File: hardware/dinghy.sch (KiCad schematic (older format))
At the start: 56 parts, among them J10 Header 1, J11 Header 2, J2 Fan 1, J3 Fan2, J4 Motor, J5 Endtemp, J6 Endstop, J7 PGM, J8 UART, J9 Power, Q1 IRLR7843PbF, Q2 IRLR7843PbF, Q3 IRLR7843PbF, SW1 SW_Push, U1 TMC2130, U2 ATMEGA1284P-AU, Y1 Crystal

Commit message: Renamed power net
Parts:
- renumbered C11 to C10, C10 to C11, J2 to J1, J11 to J10, J3 to J2, J4 to J3, J5 to J4, J6 to J5, J7 to J6, J8 to J7, J10 to J8
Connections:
- net labels added: VMot
- net labels removed: +12V, 12V, 5V, MDIAG1, M_DCEN, VM
- no-connect marks 0 -> 3
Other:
- moved on the sheet: C10

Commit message: Basic layout done.
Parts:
- R3: footprint Resistors_SMD:R_1206 -> Resistors_SMD:R_1206_HandSoldering

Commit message: Split second board of to seperate schematic
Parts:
- removed C15: 10µ, Capacitors_SMD:C_1206_HandSoldering, symbol C
- removed C7: 100µ/35V, Capacitors_SMD:CP_Elec_5x5.8, symbol CP
- removed D4: LED, LEDs:LED_1206_HandSoldering, symbol LED
- removed J2: Fan2, Connectors_JST:JST_XH_B02B-XH-A_02x2.50mm_Straight, symbol Conn_01x02_Male
- removed J5: Endstop, Connectors_JST:JST_XH_B03B-XH-A_03x2.50mm_Straight, symbol Conn_01x03_Male
- removed Q3: IRLR7843PbF, TO_SOT_Packages_SMD:TO-252-3_TabPin2, symbol Q_NMOS_GDS
- removed R14, R7: 10k, Resistors_SMD:R_1206_HandSoldering, symbol R
- removed R8: 4k7, Resistors_SMD:R_1206_HandSoldering, symbol R
- renumbered C1 to C101, C2 to C102, C3 to C103, C4 to C104, C5 to C105, C6 to C106, C8 to C107, C9 to C108, C10 to C109, C11 to C110, C12 to C111, C13 to C112, C14 to C113, D1 to D101, D2 to D102, D3 to D103, J1 to J101, J3 to J102, J4 to J103, J6 to J104, J9 to J105, J7 to J106, J8 to J107, J10 to J108, JP1 to JP101, MK1 to MK101, MK2 to MK102, MK3 to MK103, MK4 to MK104, Q1 to Q101, Q2 to Q102, R1 to R101, R2 to R102, R3 to R103, R4 to R104, R5 to R105, R6 to R106, R9 to R107, R10 to R108, R11 to R109, R12 to R110, R13 to R111, RV1 to RV101, SW1 to SW101, U1 to U101, U2 to U102, Y1 to Y101
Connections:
- net labels added: PB4
- net labels removed: FAN2
- wire segments 224 -> 236
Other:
- moved on the sheet: J103, J105, J106, J108

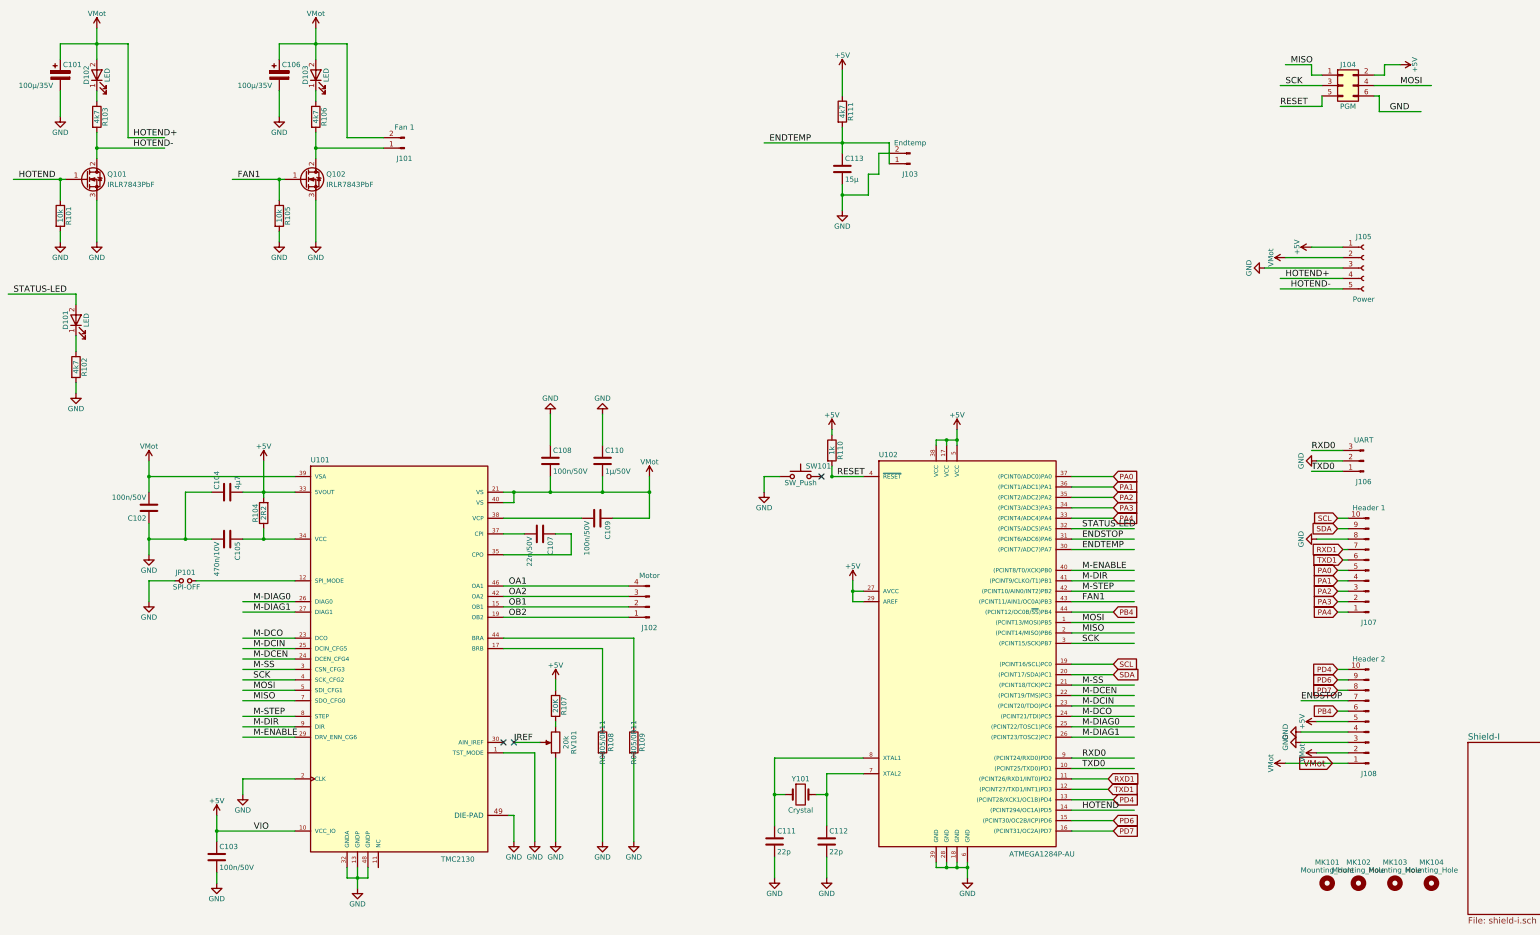
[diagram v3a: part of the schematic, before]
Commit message: Components positioned
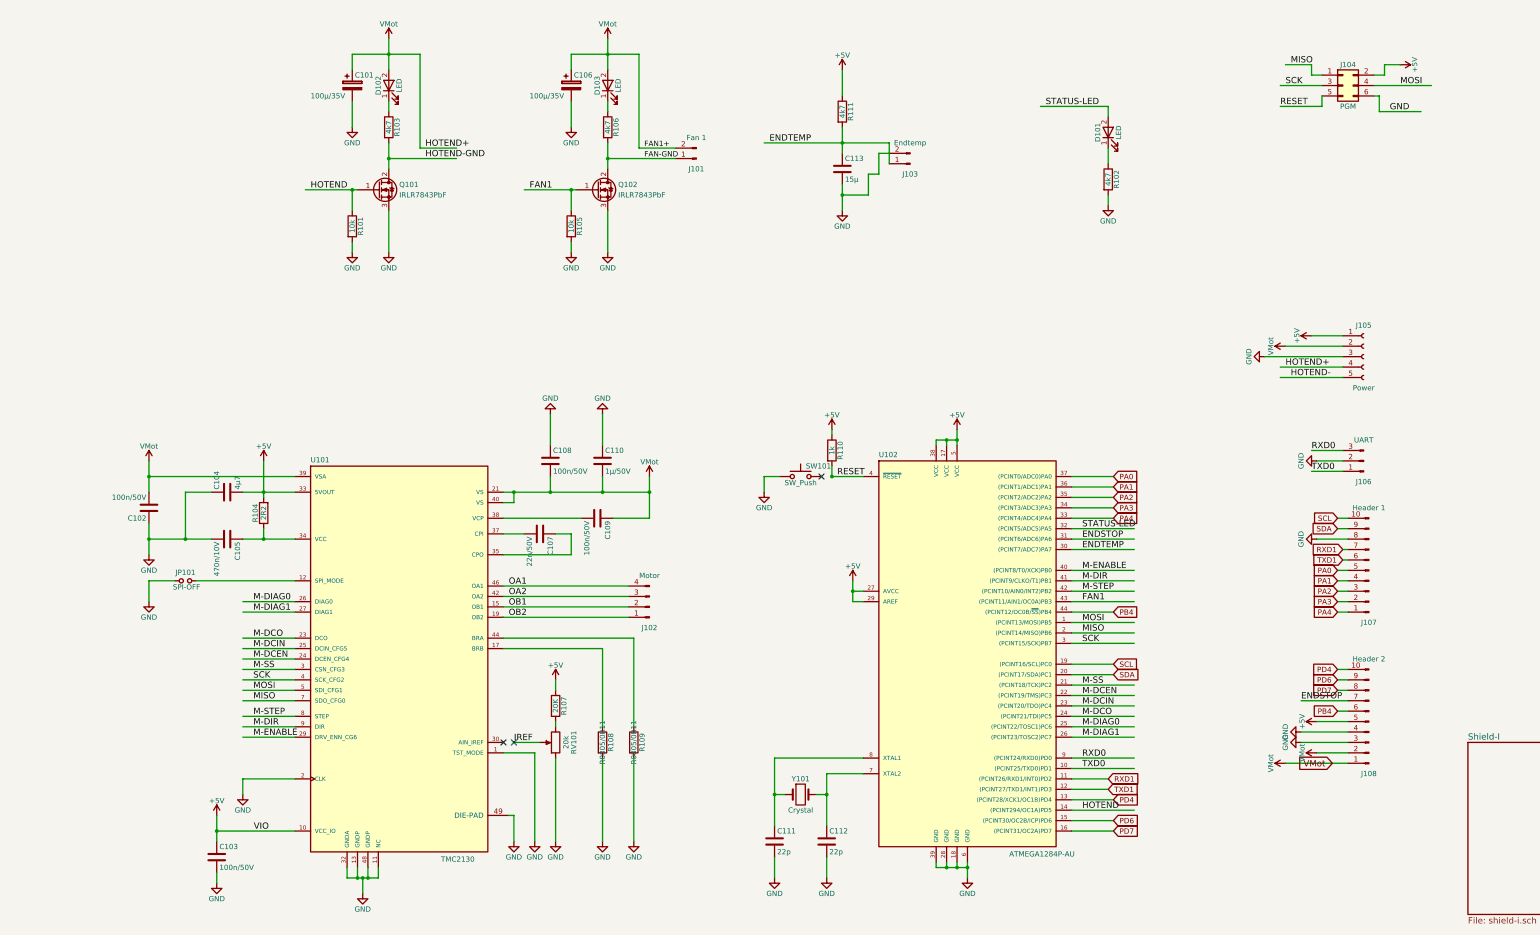
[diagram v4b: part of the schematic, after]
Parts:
- removed MK101, MK102, MK103, MK104: Mounting_Hole, Mounting_Holes:MountingHole_3mm, symbol Mounting_Hole
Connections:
- net labels added: FAN-GND, FAN1+, HOTEND-GND
- wire segments 236 -> 206
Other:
- moved on the sheet: C101, C106, D101, D102, D103, J101, J105, Q101, Q102, R101, R102, R103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
